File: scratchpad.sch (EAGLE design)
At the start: 9 parts, among them IC1 74LS14N, IC2 MCP23017SP, U1 L298

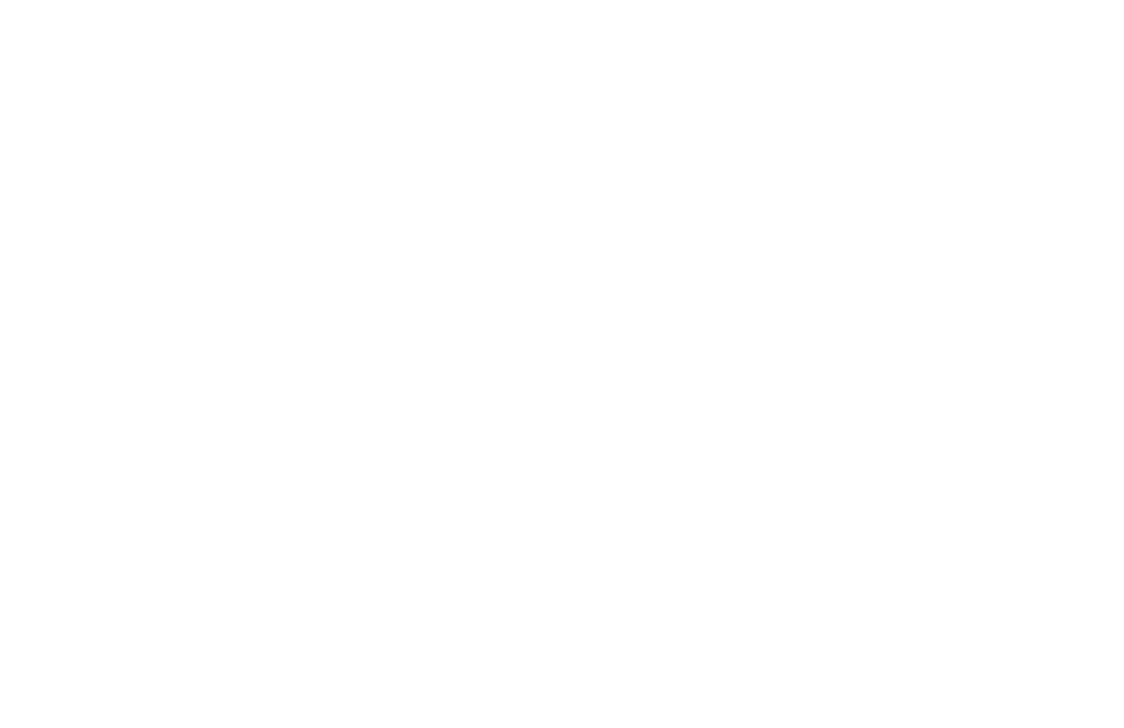
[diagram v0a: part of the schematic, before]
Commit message: cleanup and started to add servo control
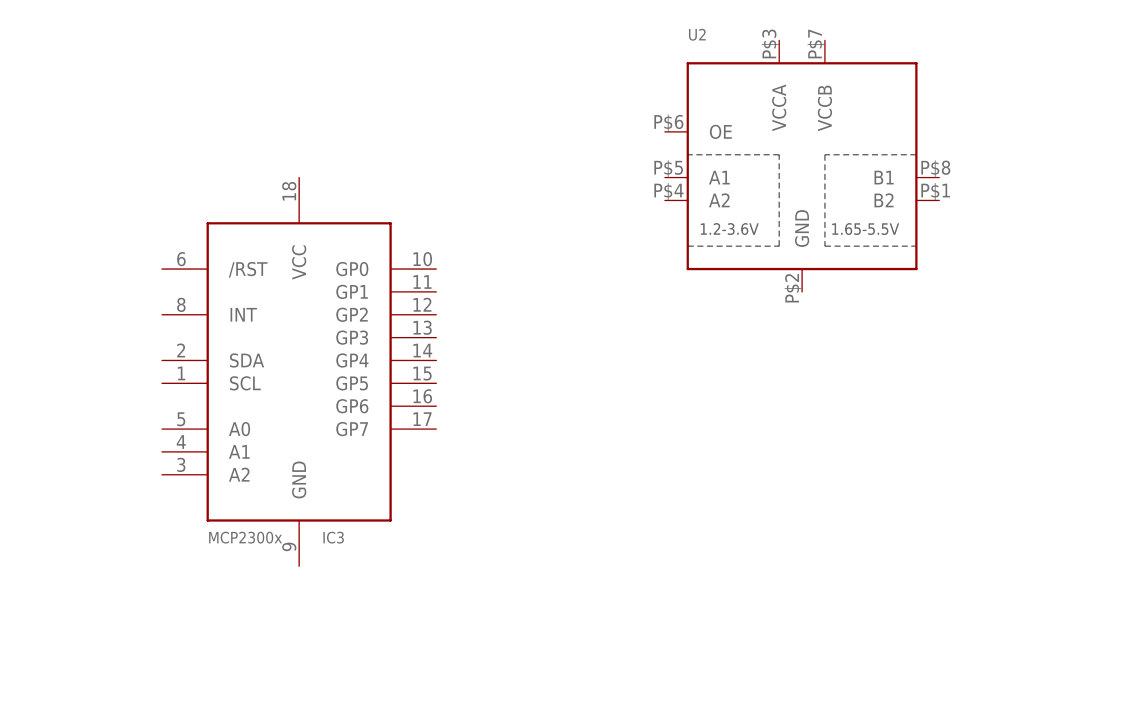
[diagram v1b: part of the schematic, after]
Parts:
- added IC3: MCP2300X/P, adafruit:MCP2300X/P
- added U2: (no value), adafruit:TXS0102
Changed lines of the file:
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@@
 <layer number="54" name="bGND_GNDA" color="1" fill="9" visible="no" active="no"/>
 <layer number="56" name="wert" color="7" fill="1" visible="no" active="no"/>
+<layer number="57" name="tCAD" color="7" fill="1" visible="no" active="no"/>
 <layer number="90" name="Modules" color="5" fill="1" visible="yes" active="yes"/>
 <layer number="91" name="Nets" color="2" fill="1" visible="yes" active="yes"/>
@@
 <layer number="108" name="tplace-old" color="10" fill="1" visible="yes" active="yes"/>
 <layer number="109" name="ref-old" color="11" fill="1" visible="yes" active="yes"/>
+<layer number="110" name="fp0" color="7" fill="1" visible="no" active="yes"/>
+<layer number="111" name="LPC17xx" color="7" fill="1" visible="yes" active="yes"/>
+<layer number="112" name="tSilk" color="7" fill="1" visible="yes" active="yes"/>
 <layer number="116" name="Patch_BOT" color="9" fill="4" visible="yes" active="yes"/>
 <layer number="121" name="_tsilk" color="7" fill="1" visible="yes" active="yes"/>
 <layer number="122" name="_bsilk" color="7" fill="1" visible="yes" active="yes"/>
+<layer number="123" name="tTestmark" color="7" fill="1" visible="no" active="yes"/>
+<layer number="124" name="bTestmark" color="7" fill="1" visible="no" active="yes"/>
 <layer number="125" name="_tNames" color="7" fill="1" visible="yes" active="yes"/>
+<layer number="126" name="_bNames" color="7" fill="1" visible="yes" active="yes"/>
+<layer number="127" name="_tValues" color="7" fill="1" visible="yes" active="yes"/>
+<layer number="128" name="_bValues" color="7" fill="1" visible="yes" active="yes"/>
+<layer number="131" name="tAdjust" color="7" fill="1" visible="no" active="yes"/>
+<layer number="132" name="bAdjust" color="7" fill="1" visible="no" active="yes"/>
 <layer number="144" name="Drill_legend" color="7" fill="1" visible="yes" active="yes"/>
+<layer number="150" name="Notes" color="7" fill="1" visible="no" active="yes"/>
 <layer number="151" name="HeatSink" color="7" fill="1" visible="yes" active="yes"/>
+<layer number="152" name="_bDocu" color="7" fill="1" visible="yes" active="yes"/>
+<layer number="153" name="FabDoc1" color="6" fill="1" visible="no" active="no"/>
+<layer number="154" name="FabDoc2" color="2" fill="1" visible="no" active="no"/>
+<layer number="155" name="FabDoc3" color="7" fill="15" visible="no" active="no"/>
 <layer number="199" name="Contour" color="7" fill="1" visible="yes" active="yes"/>
 <layer number="200" name="200bmp" color="1" fill="10" visible="yes" active="yes"/>
@@
 <layer number="223" name="223bmp" color="24" fill="1" visible="no" active="no"/>
 <layer number="224" name="224bmp" color="25" fill="1" visible="no" active="no"/>
+<layer number="248" name="Housing" color="7" fill="1" visible="yes" active="yes"/>
+<layer number="249" name="Edge" color="7" fill="1" visible="yes" active="yes"/>
 <layer number="250" name="Descript" color="3" fill="1" visible="no" active="no"/>
 <layer number="251" name="SMDround" color="12" fill="11" visible="no" active="no"/>
@@
 <part name="IC2" library="microchip" deviceset="MCP23017" device="SP"/>
 <part name="FRAME3" library="frames" deviceset="DINA4_L" device=""/>
+<part name="IC3" library="adafruit" deviceset="MCP2300X" device="/P"/>
+<part name="U2" library="adafruit" deviceset="TXS0102" device=""/>
 </parts>
 <sheets>
@@
 <instance part="FRAME3" gate="G$1" x="-12.7" y="0"/>
 <instance part="FRAME3" gate="G$2" x="149.86" y="0"/>
+<instance part="IC3" gate="G$1" x="43.18" y="119.38"/>
+<instance part="U2" gate="G$1" x="99.06" y="142.24"/>
 </instances>
 <busses>
